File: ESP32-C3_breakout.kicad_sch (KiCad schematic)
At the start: 13 parts, among them U2 ESP32-C3, Y1 40MHz

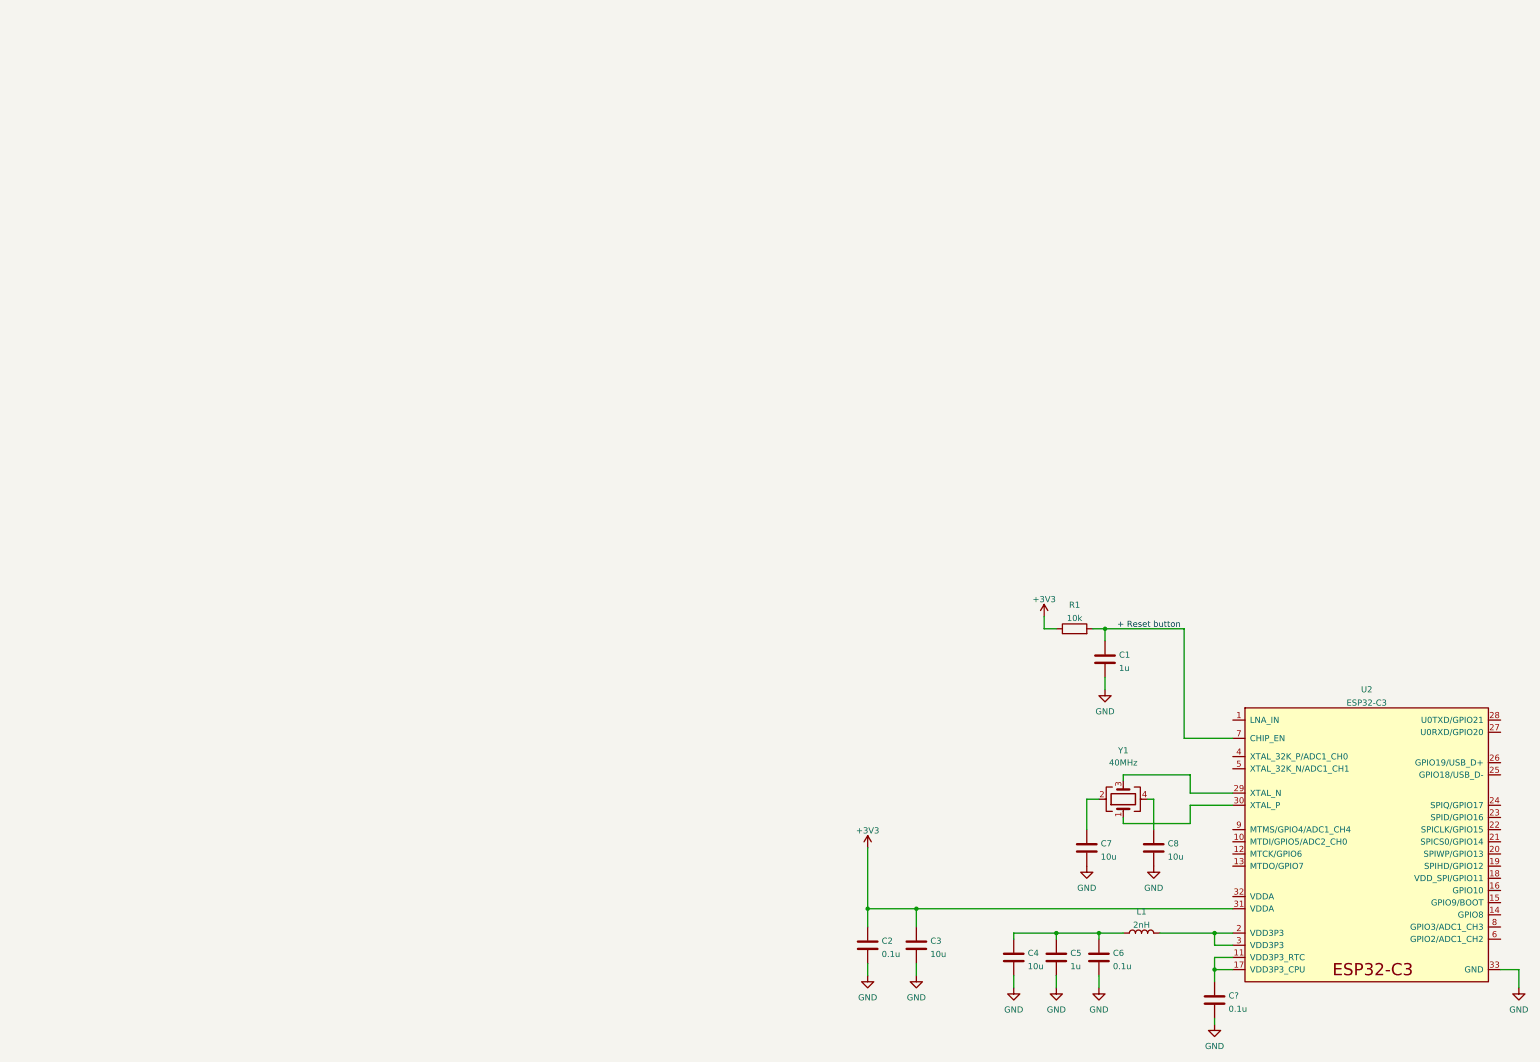
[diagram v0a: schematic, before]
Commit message: Added LDO
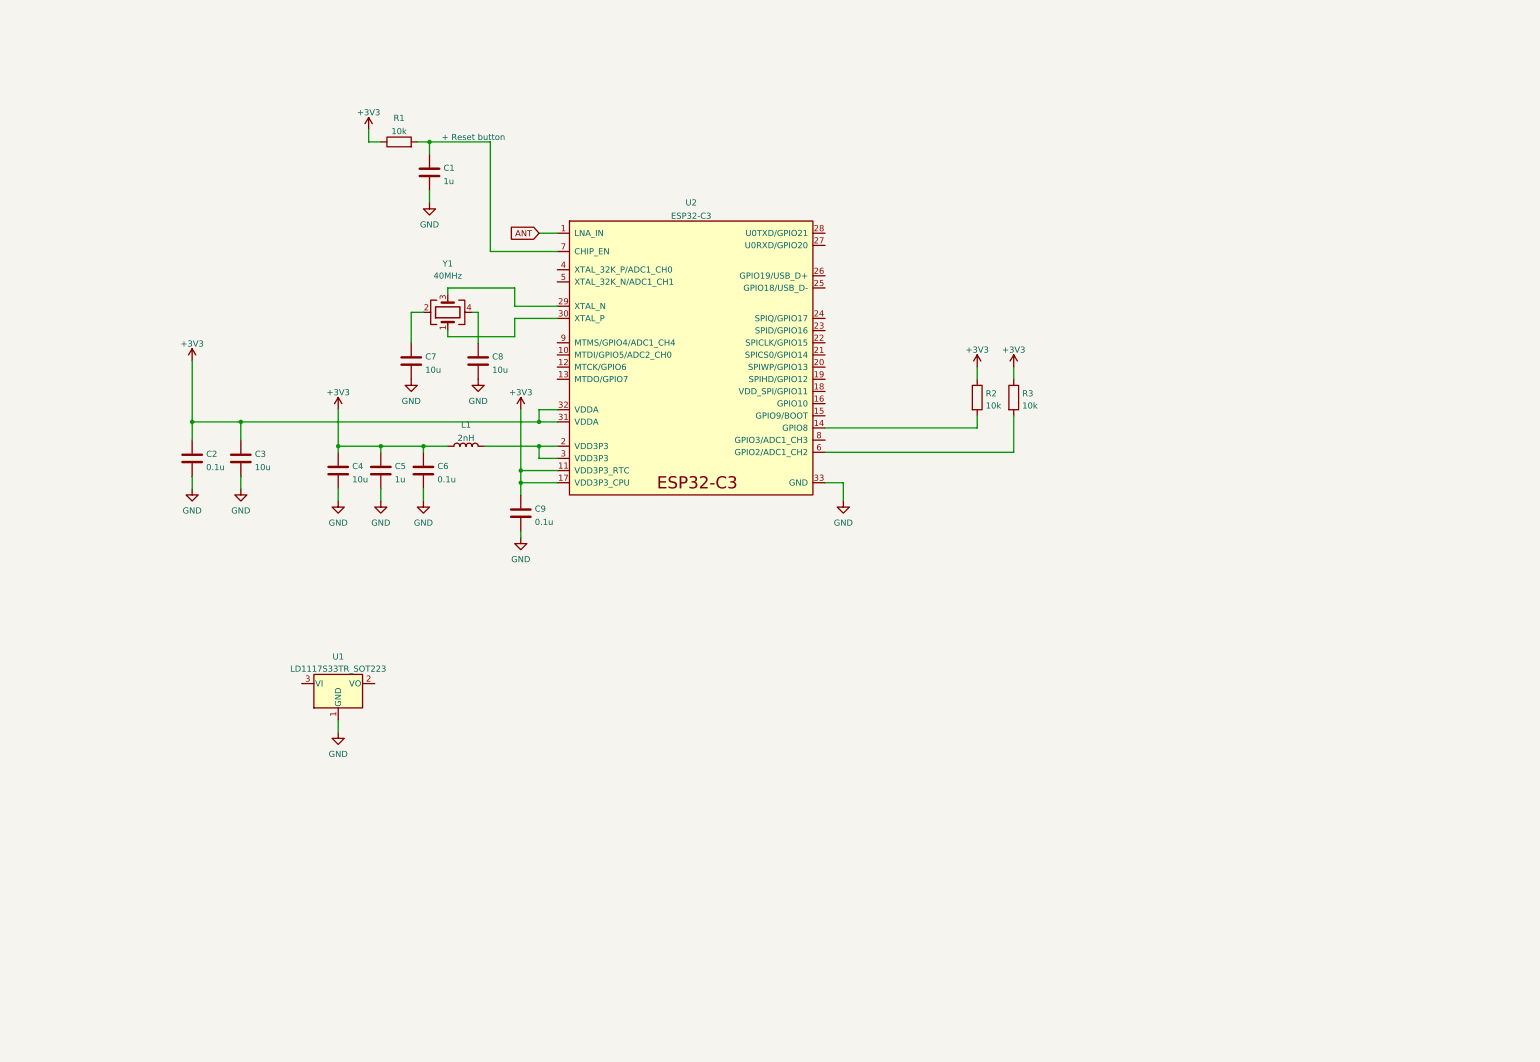
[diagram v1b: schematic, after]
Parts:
- added R2, R3: 10k, symbol Device:R
- added U1: LD1117S33TR_SOT223, Package_TO_SOT_SMD:SOT-223-3_TabPin2, symbol Regulator_Linear:LD1117S33TR_SOT223
- gave numbers to parts that had none: 1
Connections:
- net +3V3: now also C4.1, C5.1, C6.1, C9.1, L1.1, U2.11 (VDD3P3_RTC), U2.17 (VDD3P3_CPU), U2.32 (VDDA), R2.1, R3.1
- net GND: now also U1.1 (GND)
- net ANT: now reaches U2.1 (LNA_IN)
- net at U2.14 (GPIO8): now also R2.2
- net at U2.6 (GPIO2/ADC1_CH2): now also R3.2
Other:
- moved on the sheet: C1, C2, C3, C4, C5, C6, C7, C8, C9, L1, R1, U2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

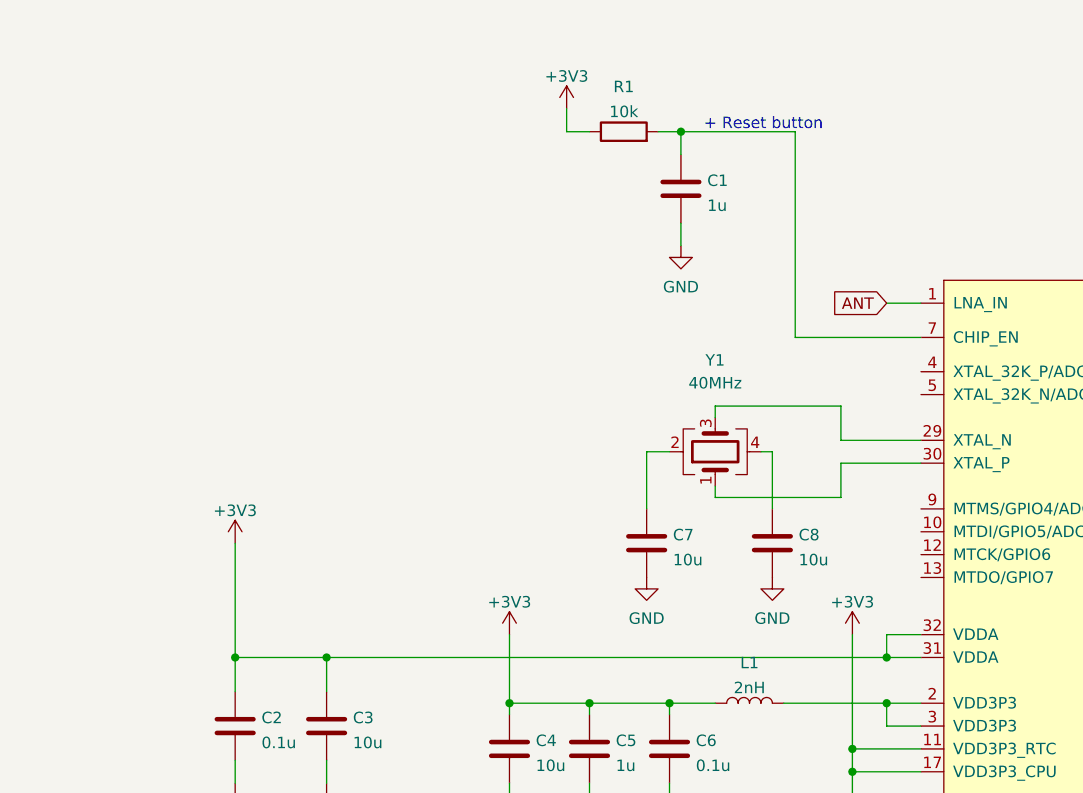
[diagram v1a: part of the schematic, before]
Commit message: Added USB-C
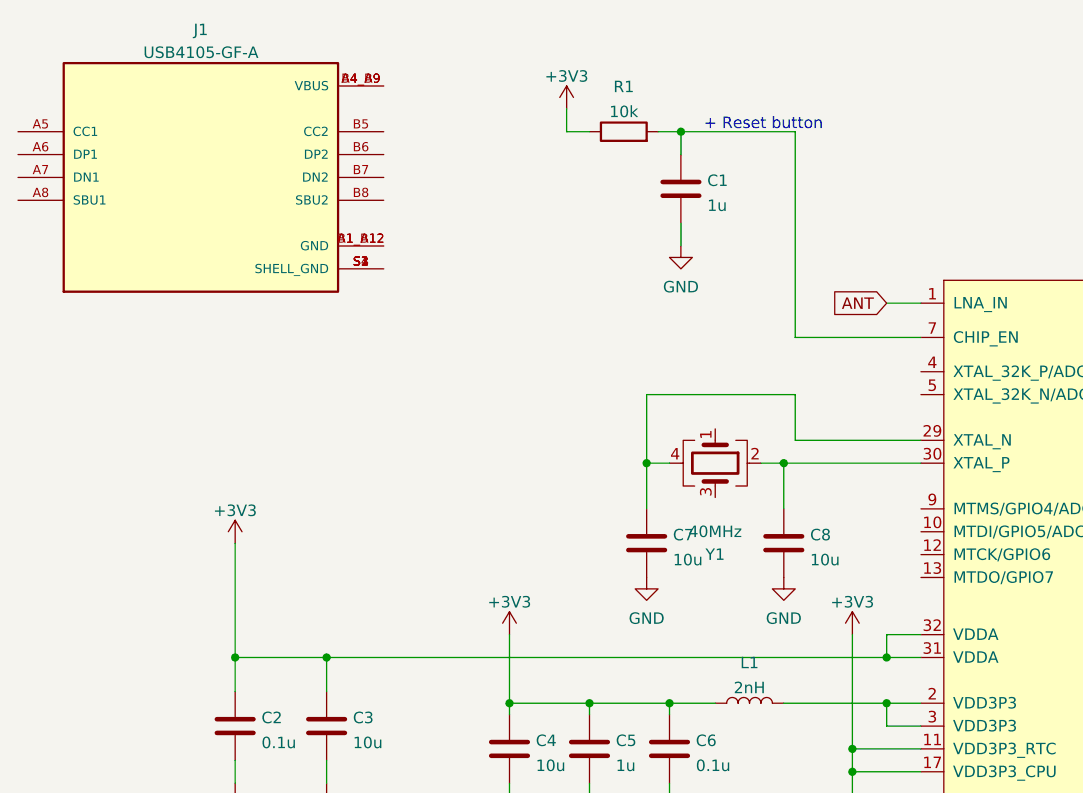
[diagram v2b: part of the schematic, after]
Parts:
- added J1: USB4105-GF-A, USB4105-GF-A:GCT_USB4105-GF-A, symbol USB4105-GF-A:USB4105-GF-A
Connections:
- net at Y1.1: no longer U2.30 (XTAL_P)
- net at Y1.2: now also C8.1, U2.30 (XTAL_P); no longer C7.1
- net at Y1.3: no longer U2.29 (XTAL_N)
- net at Y1.4: now also C7.1, U2.29 (XTAL_N); no longer C8.1
- new net: J1.A1_B12 (GND), J1.B1_A12 (GND)
- new net: J1.A4_B9 (VBUS), J1.B4_A9 (VBUS)
- new net: J1.S1 (SHELL_GND), J1.S2 (SHELL_GND), J1.S3 (SHELL_GND), J1.S4 (SHELL_GND)
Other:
- moved on the sheet: C8, Y1
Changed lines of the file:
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@@
   (junction (at 95.25 109.22) (diameter 0) (color 0 0 0 0)
   )
+  (junction (at 116.84 82.55) (diameter 0) (color 0 0 0 0)
+  )
   (junction (at 105.41 45.72) (diameter 0) (color 0 0 0 0)
   )
+  (junction (at 101.6 82.55) (diameter 0) (color 0 0 0 0)
+  )
   (junction (at 66.04 104.14) (diameter 0) (color 0 0 0 0)
   )
@@
   (junction (at 128.27 104.14) (diameter 0) (color 0 0 0 0)
   )
-  (wire (pts (xy 114.3 81.28) (xy 115.57 81.28))
-    (stroke (width 0) (type default) (color 0 0 0 0))
-  )
   (wire (pts (xy 132.08 68.58) (xy 118.11 68.58))
     (stroke (width 0) (type default) (color 0 0 0 0))
   )
-  (wire (pts (xy 123.19 76.2) (xy 123.19 80.01))
-    (stroke (width 0) (type default) (color 0 0 0 0))
-  )
   (wire (pts (xy 116.84 109.22) (xy 128.27 109.22))
     (stroke (width 0) (type default) (color 0 0 0 0))
   )
+  (wire (pts (xy 116.84 82.55) (xy 116.84 87.63))
+    (stroke (width 0) (type default) (color 0 0 0 0))
+  )
   (wire (pts (xy 118.11 45.72) (xy 118.11 68.58))
     (stroke (width 0) (type default) (color 0 0 0 0))
@@
     (stroke (width 0) (type default) (color 0 0 0 0))
   )
+  (wire (pts (xy 118.11 80.01) (xy 118.11 74.93))
+    (stroke (width 0) (type default) (color 0 0 0 0))
+  )
+  (wire (pts (xy 101.6 82.55) (xy 101.6 87.63))
+    (stroke (width 0) (type default) (color 0 0 0 0))
+  )
   (wire (pts (xy 219.71 92.71) (xy 219.71 95.25))
     (stroke (width 0) (type default) (color 0 0 0 0))
@@
     (stroke (width 0) (type default) (color 0 0 0 0))
   )
-  (wire (pts (xy 109.22 77.47) (xy 109.22 76.2))
+  (wire (pts (xy 114.3 82.55) (xy 116.84 82.55))
     (stroke (width 0) (type default) (color 0 0 0 0))
   )
@@
     (stroke (width 0) (type default) (color 0 0 0 0))
   )
-  (wire (pts (xy 123.19 80.01) (xy 132.08 80.01))
+  (wire (pts (xy 118.11 80.01) (xy 132.08 80.01))
     (stroke (width 0) (type default) (color 0 0 0 0))
   )
@@
     (stroke (width 0) (type default) (color 0 0 0 0))
   )
-  (wire (pts (xy 109.22 76.2) (xy 123.19 76.2))
+  (wire (pts (xy 101.6 74.93) (xy 101.6 82.55))
     (stroke (width 0) (type default) (color 0 0 0 0))
   )
@@
     (stroke (width 0) (type default) (color 0 0 0 0))
   )
-  (wire (pts (xy 123.19 82.55) (xy 123.19 86.36))
-    (stroke (width 0) (type default) (color 0 0 0 0))
-  )
   (wire (pts (xy 86.36 101.6) (xy 86.36 109.22))
     (stroke (width 0) (type default) (color 0 0 0 0))
   )
-  (wire (pts (xy 123.19 86.36) (xy 109.22 86.36))
-    (stroke (width 0) (type default) (color 0 0 0 0))
-  )
-  (wire (pts (xy 101.6 87.63) (xy 101.6 81.28))
-    (stroke (width 0) (type default) (color 0 0 0 0))
-  )
   (wire (pts (xy 227.33 102.87) (xy 227.33 110.49))
     (stroke (width 0) (type default) (color 0 0 0 0))
@@
     (stroke (width 0) (type default) (color 0 0 0 0))
   )
-  (wire (pts (xy 132.08 82.55) (xy 123.19 82.55))
-    (stroke (width 0) (type default) (color 0 0 0 0))
-  )
   (wire (pts (xy 128.27 111.76) (xy 132.08 111.76))
     (stroke (width 0) (type default) (color 0 0 0 0))
@@
     (stroke (width 0) (type default) (color 0 0 0 0))
   )
-  (wire (pts (xy 109.22 86.36) (xy 109.22 85.09))
-    (stroke (width 0) (type default) (color 0 0 0 0))
-  )
   (wire (pts (xy 86.36 166.37) (xy 86.36 168.91))
     (stroke (width 0) (type default) (color 0 0 0 0))
   )
-  (wire (pts (xy 115.57 81.28) (xy 115.57 87.63))
-    (stroke (width 0) (type default) (color 0 0 0 0))
-  )
   (wire (pts (xy 187.96 110.49) (xy 227.33 110.49))
     (stroke (width 0) (type default) (color 0 0 0 0))
   )
-  (wire (pts (xy 101.6 81.28) (xy 104.14 81.28))
-    (stroke (width 0) (type default) (color 0 0 0 0))
-  )
   (wire (pts (xy 187.96 105.41) (xy 219.71 105.41))
     (stroke (width 0) (type default) (color 0 0 0 0))
@@
     (stroke (width 0) (type default) (color 0 0 0 0))
   )
+  (wire (pts (xy 101.6 82.55) (xy 104.14 82.55))
+    (stroke (width 0) (type default) (color 0 0 0 0))
+  )
   (wire (pts (xy 132.08 114.3) (xy 124.46 114.3))
     (stroke (width 0) (type default) (color 0 0 0 0))
@@
   )
   (wire (pts (xy 92.71 43.18) (xy 92.71 45.72))
+    (stroke (width 0) (type default) (color 0 0 0 0))
+  )
+  (wire (pts (xy 118.11 74.93) (xy 101.6 74.93))
+    (stroke (width 0) (type default) (color 0 0 0 0))
+  )
+  (wire (pts (xy 116.84 82.55) (xy 132.08 82.55))
     (stroke (width 0) (type default) (color 0 0 0 0))
   )
@@
     (pin "2")
   )
-  (symbol (lib_id "Device:Crystal_GND24") (at 109.22 81.28 90) (unit 1)
+  (symbol (lib_id "Device:Crystal_GND24") (at 109.22 82.55 270) (unit 1)
     (in_bom yes) (on_board yes)
-    (property "Reference" "Y1" (id 0) (at 109.22 71.1231 90))
-    (property "Value" "40MHz" (id 1) (at 109.22 73.66 90))
-    (property "Footprint" "Crystal:Crystal_SMD_2016-4Pin_2.0x1.6mm" (id 2) (at 109.22 81.28 0)
-      (effects (font (size 1.27 1.27)) hide)
-    )
-    (property "Datasheet" "~" (id 3) (at 109.22 81.28 0)
+    (property "Reference" "Y1" (id 0) (at 109.22 92.7069 90))
+    (property "Value" "40MHz" (id 1) (at 109.22 90.17 90))
+    (property "Footprint" "Crystal:Crystal_SMD_2016-4Pin_2.0x1.6mm" (id 2) (at 109.22 82.55 0)
+      (effects (font (size 1.27 1.27)) hide)
+    )
+    (property "Datasheet" "~" (id 3) (at 109.22 82.55 0)
       (effects (font (size 1.27 1.27)) hide)
     )
@@
     (pin "2")
   )
-  (symbol (lib_id "power:GND") (at 115.57 95.25 0) (unit 1)
-    (in_bom yes) (on_board yes) (fields_autoplaced)
-    (property "Reference" "#PWR011" (id 0) (at 115.57 101.6 0)
-      (effects (font (size 1.27 1.27)) hide)
-    )
-    (property "Value" "GND" (id 1) (at 115.57 99.8125 0))
-    (property "Footprint" "" (id 2) (at 115.57 95.25 0)
-      (effects (font (size 1.27 1.27)) hide)
-    )
-    (property "Datasheet" "" (id 3) (at 115.57 95.25 0)
+  (symbol (lib_id "power:GND") (at 116.84 95.25 0) (unit 1)
+    (in_bom yes) (on_board yes) (fields_autoplaced)
+    (property "Reference" "#PWR011" (id 0) (at 116.84 101.6 0)
+      (effects (font (size 1.27 1.27)) hide)
+    )
+    (property "Value" "GND" (id 1) (at 116.84 99.8125 0))
+    (property "Footprint" "" (id 2) (at 116.84 95.25 0)
+      (effects (font (size 1.27 1.27)) hide)
+    )
+    (property "Datasheet" "" (id 3) (at 116.84 95.25 0)
       (effects (font (size 1.27 1.27)) hide)
     )
@@
     (pin "2")
   )
-  (symbol (lib_id "Device:C") (at 115.57 91.44 0) (unit 1)
-    (in_bom yes) (on_board yes) (fields_autoplaced)
-    (property "Reference" "C8" (id 0) (at 118.491 90.5315 0)
-      (effects (font (size 1.27 1.27)) (justify left))
-    )
-    (property "Value" "10u" (id 1) (at 118.491 93.3066 0)
-      (effects (font (size 1.27 1.27)) (justify left))
-    )
-    (property "Footprint" "Capacitor_SMD:C_0603_1608Metric" (id 2) (at 116.5352 95.25 0)
-      (effects (font (size 1.27 1.27)) hide)
-    )
-    (property "Datasheet" "~" (id 3) (at 115.57 91.44 0)
+  (symbol (lib_id "Device:C") (at 116.84 91.44 0) (unit 1)
+    (in_bom yes) (on_board yes) (fields_autoplaced)
+    (property "Reference" "C8" (id 0) (at 119.761 90.5315 0)
+      (effects (font (size 1.27 1.27)) (justify left))
+    )
+    (property "Value" "10u" (id 1) (at 119.761 93.3066 0)
+      (effects (font (size 1.27 1.27)) (justify left))
+    )
+    (property "Footprint" "Capacitor_SMD:C_0603_1608Metric" (id 2) (at 117.8052 95.25 0)
+      (effects (font (size 1.27 1.27)) hide)
+    )
+    (property "Datasheet" "~" (id 3) (at 116.84 91.44 0)
       (effects (font (size 1.27 1.27)) hide)
     )
@@
     )
     (pin "1")
+  )
+  (symbol (lib_id "USB4105-GF-A:USB4105-GF-A") (at 52.07 50.8 0) (unit 1)
+    (in_bom yes) (on_board yes) (fields_autoplaced)
+    (property "Reference" "J1" (id 0) (at 52.07 34.4002 0))
+    (property "Value" "USB4105-GF-A" (id 1) (at 52.07 36.9371 0))
+    (property "Footprint" "USB4105-GF-A:GCT_USB4105-GF-A" (id 2) (at 52.07 50.8 0)
+      (effects (font (size 1.27 1.27)) (justify left bottom) hide)
+    )
+    (property "Datasheet" "" (id 3) (at 52.07 50.8 0)
+      (effects (font (size 1.27 1.27)) (justify left bottom) hide)
+    )
+    (property "PARTREV" "A3" (id 4) (at 52.07 50.8 0)
+      (effects (font (size 1.27 1.27)) (justify left bottom) hide)
+    )
+    (property "MANUFACTURER" "GCT" (id 5) (at 52.07 50.8 0)
+      (effects (font (size 1.27 1.27)) (justify left bottom) hide)
+    )
+    (property "MAXIMUM_PACKAGE_HEIGHT" "3.31 mm" (id 6) (at 52.07 50.8 0)
+      (effects (font (size 1.27 1.27)) (justify left bottom) hide)
+    )
+    (property "STANDARD" "Manufacturer Recommendations" (id 7) (at 52.07 50.8 0)
+      (effects (font (size 1.27 1.27)) (justify left bottom) hide)
+    )
+    (pin "A1_B12")
+    (pin "A4_B9")
+    (pin "A5")
+    (pin "A6")
+    (pin "A7")
+    (pin "A8")
+    (pin "B1_A12")
+    (pin "B4_A9")
+    (pin "B5")
+    (pin "B6")
+    (pin "B7")
+    (pin "B8")
+    (pin "S1")
+    (pin "S2")
+    (pin "S3")
+    (pin "S4")
   )
   (symbol (lib_id "power:GND") (at 104.14 120.65 0) (unit 1)
@@
       (reference "C9") (unit 1) (value "0.1u") (footprint "Capacitor_SMD:C_0603_1608Metric")
     )
+    (path "/940b6164-5d05-4114-9128-b3f4431ad594"
+      (reference "J1") (unit 1) (value "USB4105-GF-A") (footprint "USB4105-GF-A:GCT_USB4105-GF-A")
+    )
     (path "/79945d18-f992-4a80-8220-05e4a004f9b2"

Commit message: General improvements
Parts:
- removed R2: 10k, symbol Device:R
- added C10, C12: 10u, Capacitor_SMD:C_0603_1608Metric, symbol Device:C
- added C11: 1u, Capacitor_SMD:C_0603_1608Metric, symbol Device:C
- added J2, J3: Conn_01x11_Male, Connector_PinHeader_2.54mm:PinHeader_1x11_P2.54mm_Vertical, symbol Connector:Conn_01x11_Male
- added R4, R5: 5k1, Resistor_SMD:R_0603_1608Metric, symbol Device:R
- added SW1, SW2: SW_Push, Button_Switch_SMD:SW_SPST_FSMSM, symbol Switch:SW_Push
- added U3: WE-TVS-82400102, Package_TO_SOT_SMD:SOT-23-6, symbol Power_Protection:WE-TVS-82400102
- R3: footprint (none) -> Resistor_SMD:R_0603_1608Metric
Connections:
- net +3V3: now also U1.2 (VO), C11.1, C12.1
- net GND: now also J1.A1_B12 (GND), J1.B1_A12 (GND), C10.2, C11.2, C12.2, R4.2, R5.2, SW1.2, SW2.2, U3.2
- net EN: now reaches C1.1, R1.2, U2.7 (CHIP_EN)
- net EN: now also J3.1 (Pin_1), SW1.1
- net VDD: now reaches J1.A4_B9 (VBUS), J1.B4_A9 (VBUS)
- net VDD: now also U1.3 (VI), C10.1, U3.5
- net at J1.A5 (CC1): now also R4.1
- net at J1.A6 (DP1): now also J1.B6 (DP2), U3.1
- net at J1.A7 (DN1): now also J1.B7 (DN2), U3.3
- net at J1.B5 (CC2): now also R5.1
- net BOOT: now reaches U2.15 (GPIO9/BOOT)
- net BOOT: now also SW2.1
- net USB_D-: now reaches U2.25 (GPIO18/USB_D-)
- net USB_D-: now also U3.4
- net USB_D+: now reaches U2.26 (GPIO19/USB_D+)
- net USB_D+: now also U3.6
- new net GPIO0: J2.1 (Pin_1)
- new net GPIO1: J2.2 (Pin_2)
- new net GPIO10: J2.11 (Pin_11)
- new net GPIO2: J2.3 (Pin_3)
- new net GPIO3: J2.4 (Pin_4)
- new net GPIO4: J2.5 (Pin_5)
- new net GPIO5: J2.6 (Pin_6)
- new net GPIO6: J2.7 (Pin_7)
- new net GPIO7: J2.8 (Pin_8)
- new net GPIO8: J2.9 (Pin_9)
- new net GPIO9: J2.10 (Pin_10)
- new net RX: J3.2 (Pin_2)
- new net TX: J3.3 (Pin_3)
- no-connect marks 0 -> 3
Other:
- note added: "3V3 Voltage regulator"
- note added: "Reset & Boot"
- note added: "USB-C & ESD protection"
- note removed: "+ Reset button"
- moved on the sheet: C1, C2, C3, C4, C5, C6, C7, C8, C9, J1, L1, R1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
